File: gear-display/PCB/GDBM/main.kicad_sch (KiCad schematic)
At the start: 22 parts

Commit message: new features
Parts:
- added R?: R_0603_22k_1%, KD_Resistor:R_0603_1608Metric, symbol KD_Resistor:R_0603_22k_1%
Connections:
- net CLK_5V is gone; now on net SCLK: X?.3 (SCK)
- net MISO_5V is gone; now on net MISO: X?.1 (MISO)
- net MOSI_5V is gone; now on net MOSI: X?.4 (MOSI)
- net I2C_SCL renamed SCL
- net I2C_SDA renamed SDA
- net VREF_4.096V: no longer names the net of U?.42 (AREF)
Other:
- note added: "PWM"

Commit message: updates
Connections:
- net +3V3 renamed +5V

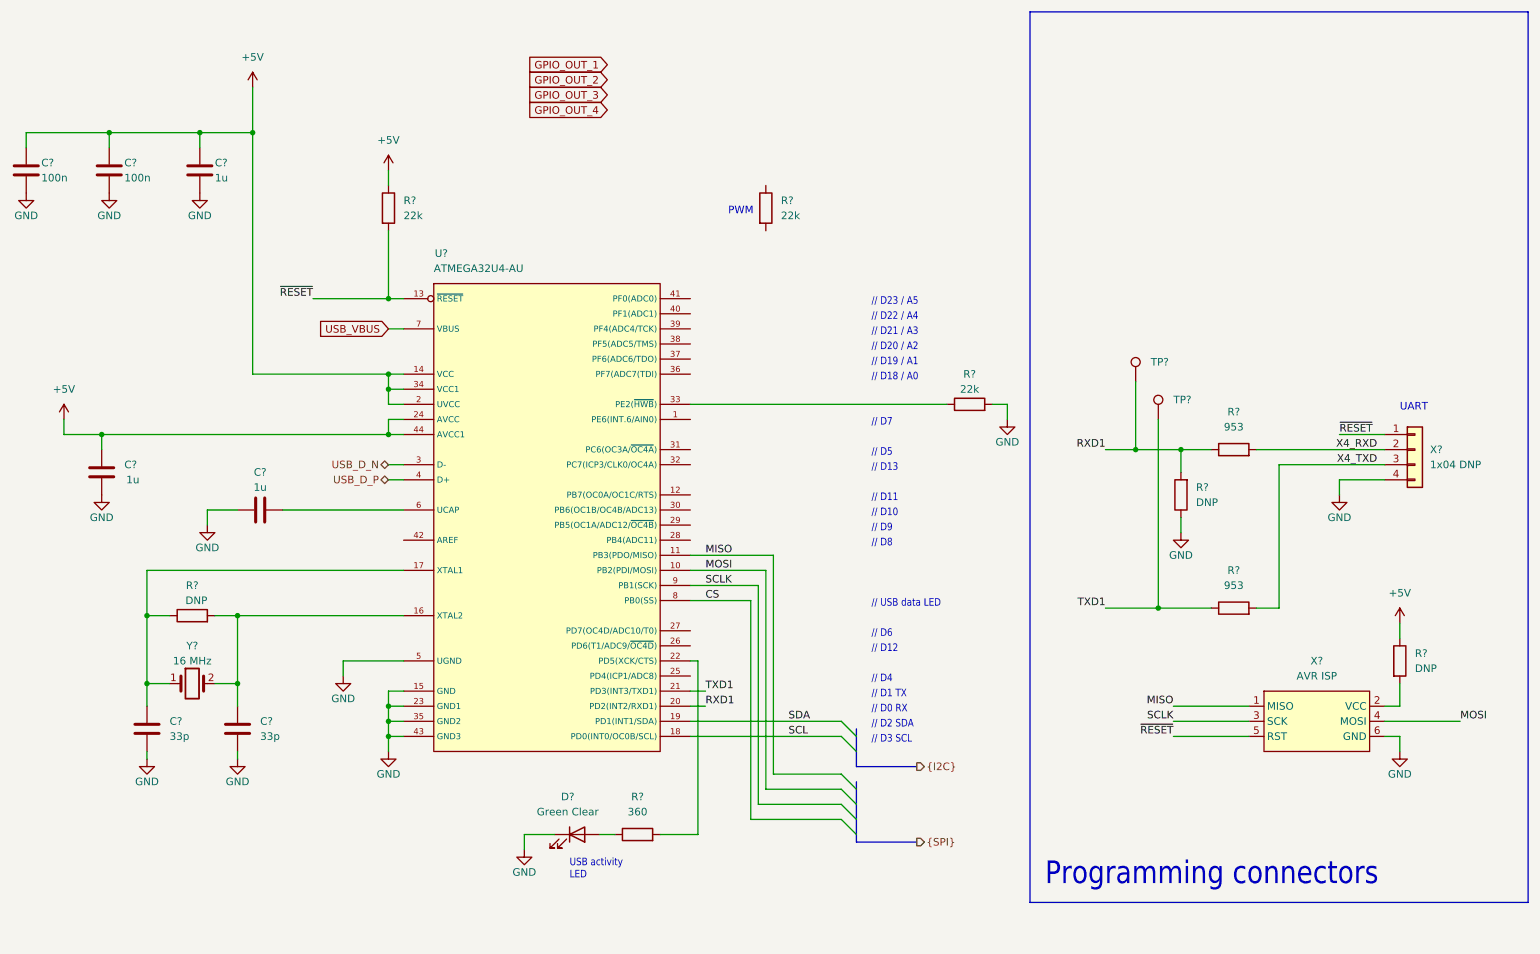
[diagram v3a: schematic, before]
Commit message: changed to match simhub conf
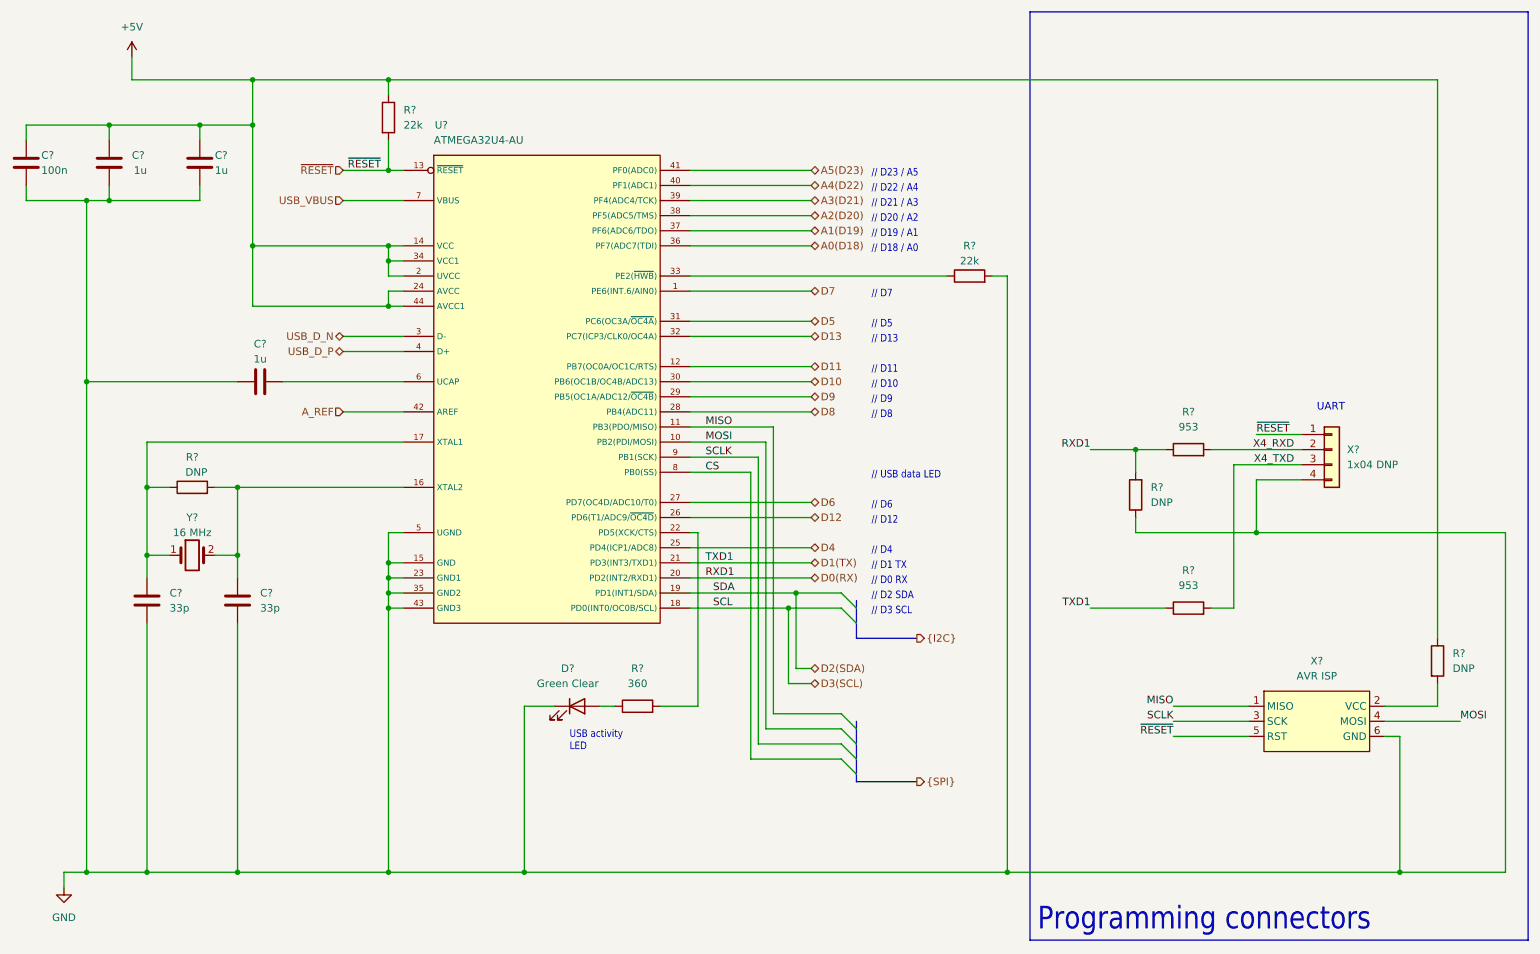
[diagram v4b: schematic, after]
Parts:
- removed C?: C_0603_100n_X7R_50V, KD_Capacitor:C_0603_1608Metric, symbol KD_Capacitor:C_0603_100n_X7R_50V
- removed R?: R_0603_22k_1%, KD_Resistor:R_0603_1608Metric, symbol KD_Resistor:R_0603_22k_1%
- removed TP? (x2): TestPoint_2.5mm_Round, KD_Connector_Pads:TestPoint_Pad_D2.5mm, symbol KD_Connector_Pads:TestPoint_2.5mm_Round
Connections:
- net D7: now reaches U?.1 (PE6(INT.6/AIN0))
- net D11: now reaches U?.12 (PB7(OC0A/OC1C/RTS))
- net D4: now reaches U?.25 (PD4(ICP1/ADC8))
- net D12: now reaches U?.26 (PD6(T1/ADC9/~{OC4D}))
- net D6: now reaches U?.27 (PD7(OC4D/ADC10/T0))
- net D8: now reaches U?.28 (PB4(ADC11))
- net D9: now reaches U?.29 (PB5(OC1A/ADC12/~{OC4B}))
- net D10: now reaches U?.30 (PB6(OC1B/OC4B/ADC13))
- net D5: now reaches U?.31 (PC6(OC3A/~{OC4A}))
- net D13: now reaches U?.32 (PC7(ICP3/CLK0/OC4A))
- net A0(D18): now reaches U?.36 (PF7(ADC7(TDI))
- net A1(D19): now reaches U?.37 (PF6(ADC6/TDO))
- net A2(D20): now reaches U?.38 (PF5(ADC5/TMS))
- net A3(D21): now reaches U?.39 (PF4(ADC4/TCK))
- net A4(D22): now reaches U?.40 (PF1(ADC1))
- net A5(D23): now reaches U?.41 (PF0(ADC0))
- net A_REF: now reaches U?.42 (AREF)
- net RXD1 renamed D0(RX)
- net SCL renamed D3(SCL)
- net SDA renamed D2(SDA)
- net TXD1 renamed D1(TX)
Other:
- note removed: "PWM"
- moved on the sheet: C?, D?, R?, U?, X?, Y?

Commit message: rikki
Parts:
- removed C?: C_0603_100n_X7R_50V, KD_Capacitor:C_0603_1608Metric, symbol KD_Capacitor:C_0603_100n_X7R_50V
- removed R? (x2): R_0603_953_1%, KD_Resistor:R_0603_1608Metric, symbol KD_Resistor:R_0603_953_1%
- added C6: C_0603_100n_X7R_100V, KD_Capacitor:C_0603_1608Metric, symbol KD_Capacitor:C_0603_100n_X7R_100V
- added R6, R7: R_0603_360_1%, KD_Resistor:RESC1608X55N, symbol KD_Resistor:R_0603_360_1%
- R1: renamed from R?; footprint KD_Resistor:R_0805_2012Metric_DNP -> KD_Resistor:RESC2012X60N_DNP
- R2, R3, R4: renamed from R?; footprint KD_Resistor:R_0603_1608Metric -> KD_Resistor:RESC1608X55N
- R5: renamed from R?; footprint KD_Resistor:R_0603_1608Metric_DNP -> KD_Resistor:RESC1608X55N_DNP
- R8: renamed from R?; footprint KD_Resistor:R_0402_1005Metric_DNP -> KD_Resistor:RESC1005X40N
- gave numbers to parts that had none: 10
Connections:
- net +5V: now also C6.1
- net D0(RX): now also R6.1
- net D1(TX): now also R7.1
- net GND: now also C6.2
- net X4_RXD: now also R6.2
- net X4_TXD: now also R7.2
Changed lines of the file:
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@@
   (title_block
     (title "Gear Display Board")
-    (date "2022-08-07")
+    (date "2022-08-13")
     (rev "1.0")
     (company "Kallio Designs Oy")
     (comment 1 "Teemu Latonen")
-    (comment 2 "ASSEMBLY_PN")
-    (comment 3 "PCB_PN")
+    (comment 2 "000064")
+    (comment 3 "000065")
   )

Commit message: PSU and LED powering changed
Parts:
- C10, C6, C8: footprint KD_Capacitor:C_0603_1608Metric -> KD_Capacitor:CAPC1608X90N
- C11, C7, C9: footprint KD_Capacitor:C_0805_2012Metric -> KD_Capacitor:CAPC2012X135N
